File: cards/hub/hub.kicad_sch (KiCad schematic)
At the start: 28 parts, among them J1 USB_B, J2 BUS, J3 BUS

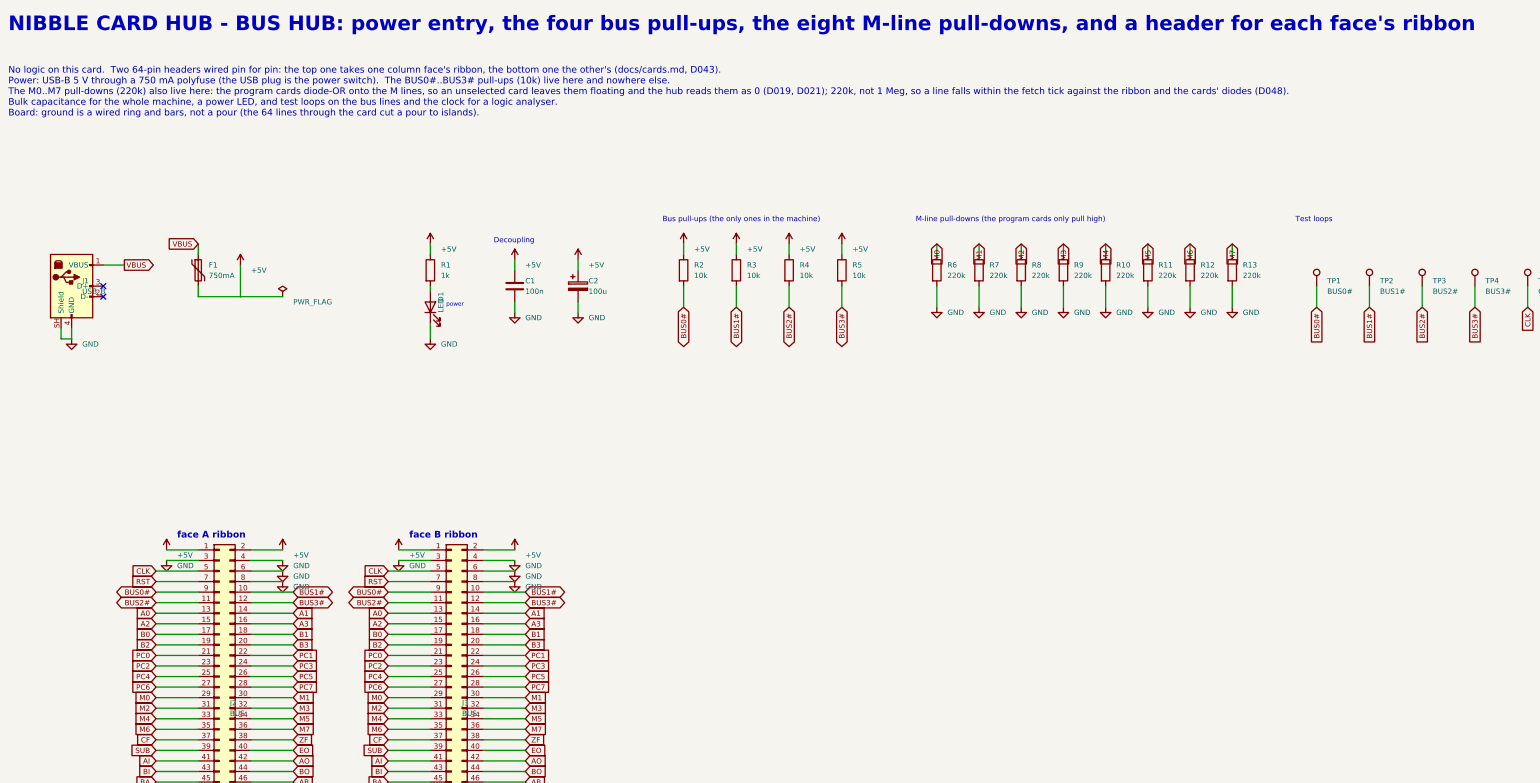
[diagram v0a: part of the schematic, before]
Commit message: Hub: bench-supply screw terminal and a 1.5 A polyfuse (D052)
The machine as built draws up to about 1.2 A (281 LEDs behind 1k, plus
the pull-ups), more than the 750 mA fuse and a computer's USB port were
ever going to carry. The hub now takes 5 V from a 5.08 mm screw terminal
on its left edge (the Kungber bench supply, 5.0 V with the limit at
1.5 A) as well as from the USB-B socket, both through a Bel 0ZRE0150FF
1.5 A polyfuse.

Routed with freerouting 2.4.1: 1.9 put an M5 via inside the 0.35 mm
bundle of the 64 bus lines and shorted M4/M5/M7 on two runs. KiCad DRC
and the JLCPCB-minimum DRC (0.127 track/space, 0.3/0.5 via, 0.5
hole-to-hole) both report no errors and nothing unconnected. Renders
checked. Parts table in order-1.md regenerated from bom.py (it had
also drifted from earlier card changes); bring-up, cards.md, README and
DECISIONS updated. The sim netlist is untouched (both parts are
sim=False), so the whole-machine proof stands.

Co-Authored-By: Claude Fable 5.1 <noreply@anthropic.com>
Claude-Session: https://claude.ai/code/session_01RktbhdQjDu7SpFpvkevyUU
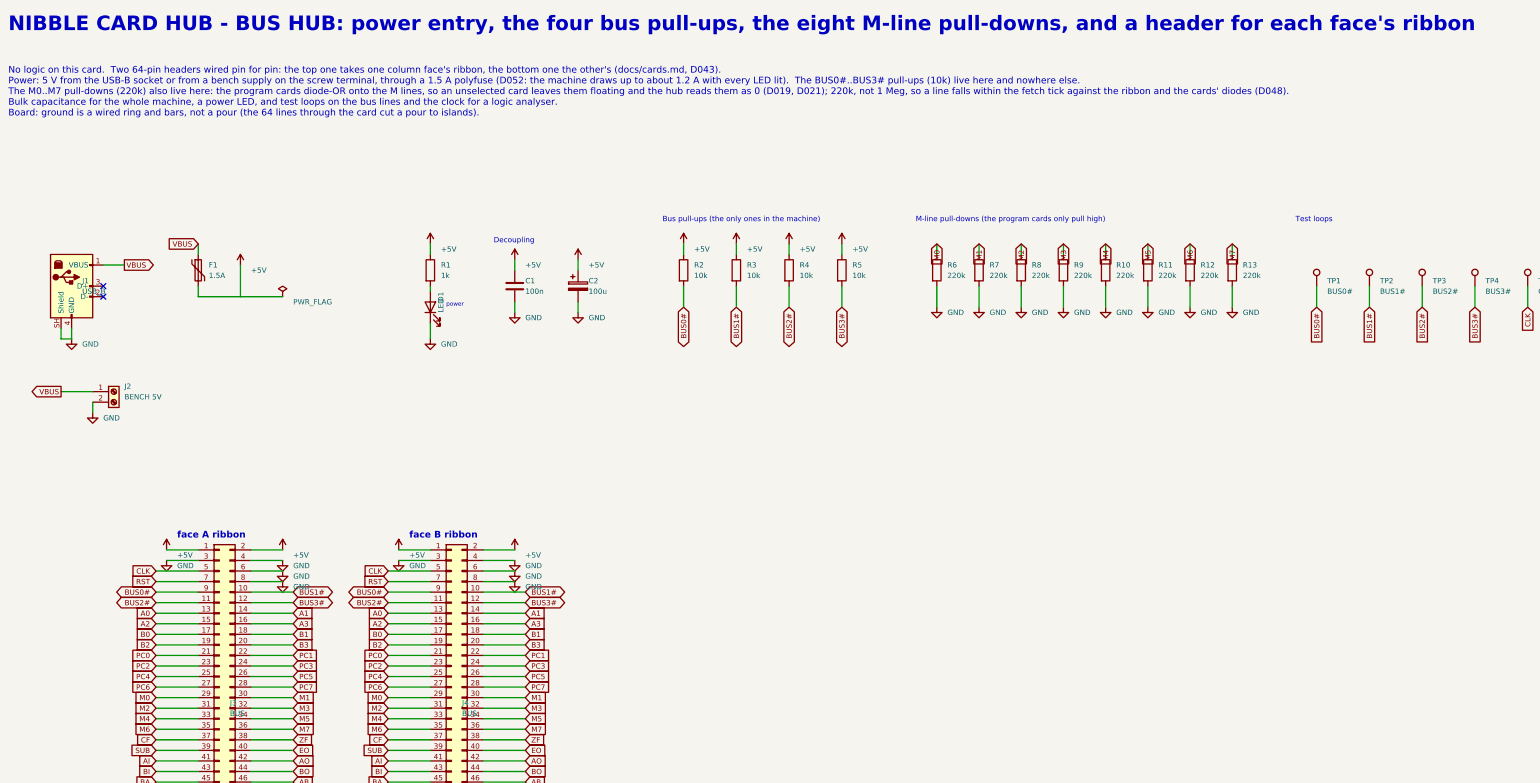
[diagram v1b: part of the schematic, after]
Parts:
- removed J2: BUS, Connector_IDC:IDC-Header_2x32_P2.54mm_Vertical, symbol Connector_Generic:Conn_02x32_Odd_Even
- added J2: BENCH 5V, TerminalBlock_Phoenix:TerminalBlock_Phoenix_MKDS-1,5-2-5.08_1x02_P5.08mm_Horizontal, symbol Connector:Screw_Terminal_01x02
- added J4: BUS, Connector_IDC:IDC-Header_2x32_P2.54mm_Vertical, symbol Connector_Generic:Conn_02x32_Odd_Even
- F1: value 750mA -> 1.5A; footprint Fuse:Fuse_BelFuse_0ZRE0075FF_L11.5mm_W4.8mm -> Fuse:Fuse_BelFuse_0ZRE0150FF_L23.4mm_W5.3mm
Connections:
- net +5V: now also J4.1 (Pin_1), J4.2 (Pin_2), J4.63 (Pin_63)
- net A0: now also J4.13 (Pin_13)
- net A1: now also J4.14 (Pin_14)
- net A2: now also J4.15 (Pin_15)
- net A3: now also J4.16 (Pin_16)
- net AB: now also J4.46 (Pin_46)
- net AI: now also J4.41 (Pin_41)
- net AO: now also J4.42 (Pin_42)
- net B0: now also J4.17 (Pin_17)
- net B1: now also J4.18 (Pin_18)
- net B2: now also J4.19 (Pin_19)
- net B3: now also J4.20 (Pin_20)
- net BA: now also J4.45 (Pin_45)
- net BI: now also J4.43 (Pin_43)
- net BO: now also J4.44 (Pin_44)
- net BUS0#: now also J4.9 (Pin_9)
- net BUS1#: now also J4.10 (Pin_10)
- net BUS2#: now also J4.11 (Pin_11)
- net BUS3#: now also J4.12 (Pin_12)
- net CF: now also J4.37 (Pin_37)
- net CLK: now also J4.5 (Pin_5)
- net EO: now also J4.40 (Pin_40)
- net F0: now also J4.60 (Pin_60)
- net F1: now also J4.61 (Pin_61)
- net FI: now also J4.52 (Pin_52)
- net GND: now also J2.2 (Pin_2), J4.3 (Pin_3), J4.4 (Pin_4), J4.6 (Pin_6), J4.64 (Pin_64), J4.8 (Pin_8)
- net HLT: now also J4.53 (Pin_53)
- net II: now also J4.49 (Pin_49)
- net INP: now also J4.62 (Pin_62)
- net IO: now also J4.48 (Pin_48)
- net M0: now also J4.29 (Pin_29)
- net M1: now also J4.30 (Pin_30)
- net M2: now also J4.31 (Pin_31)
- net M3: now also J4.32 (Pin_32)
- net M4: now also J4.33 (Pin_33)
- net M5: now also J4.34 (Pin_34)
- net M6: now also J4.35 (Pin_35)
- net M7: now also J4.36 (Pin_36)
- net MAI: now also J4.54 (Pin_54)
- net MI: now also J4.55 (Pin_55)
- net MO: now also J4.56 (Pin_56)
- net OI: now also J4.47 (Pin_47)
- net ONE: now also J4.59 (Pin_59)
- net PC0: now also J4.21 (Pin_21)
- net PC1: now also J4.22 (Pin_22)
- net PC2: now also J4.23 (Pin_23)
- net PC3: now also J4.24 (Pin_24)
- net PC4: now also J4.25 (Pin_25)
- net PC5: now also J4.26 (Pin_26)
- net PC6: now also J4.27 (Pin_27)
- net PC7: now also J4.28 (Pin_28)
- net PCE: now also J4.50 (Pin_50)
- net PCL: now also J4.51 (Pin_51)
- net RST: now also J4.7 (Pin_7)
- net SUB: now also J4.39 (Pin_39)
- net VBUS: now also J2.1 (Pin_1)
- net WRH: now also J4.58 (Pin_58)
- net WRL: now also J4.57 (Pin_57)
- net ZF: now also J4.38 (Pin_38)
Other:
- note added: "No logic on this card. Two 64-pin headers wired pin for pin: the top one takes one column face's ribbon, the bottom one the other's (docs/cards.md, D043). Power: 5 V from the USB-B socket or from a bench supply on the screw terminal, through a 1.5 A polyfuse (D052: the machine draws up to about 1.2 A with every LED lit). The BUS0#..BUS3# pull-ups (10k) live here and nowhere else. The M0..M7 pull-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"
- note removed: "No logic on this card. Two 64-pin headers wired pin for pin: the top one takes one column face's ribbon, the bottom one the other's (docs/cards.md, D043). Power: USB-B 5 V through a 750 mA polyfuse (the USB plug is the power switch). The BUS0#..BUS3# pull-ups (10k) live here and nowhere else. The M0..M7 pull-downs (220k) also live here: the program cards diode-OR onto the M lines, so an unselecte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"

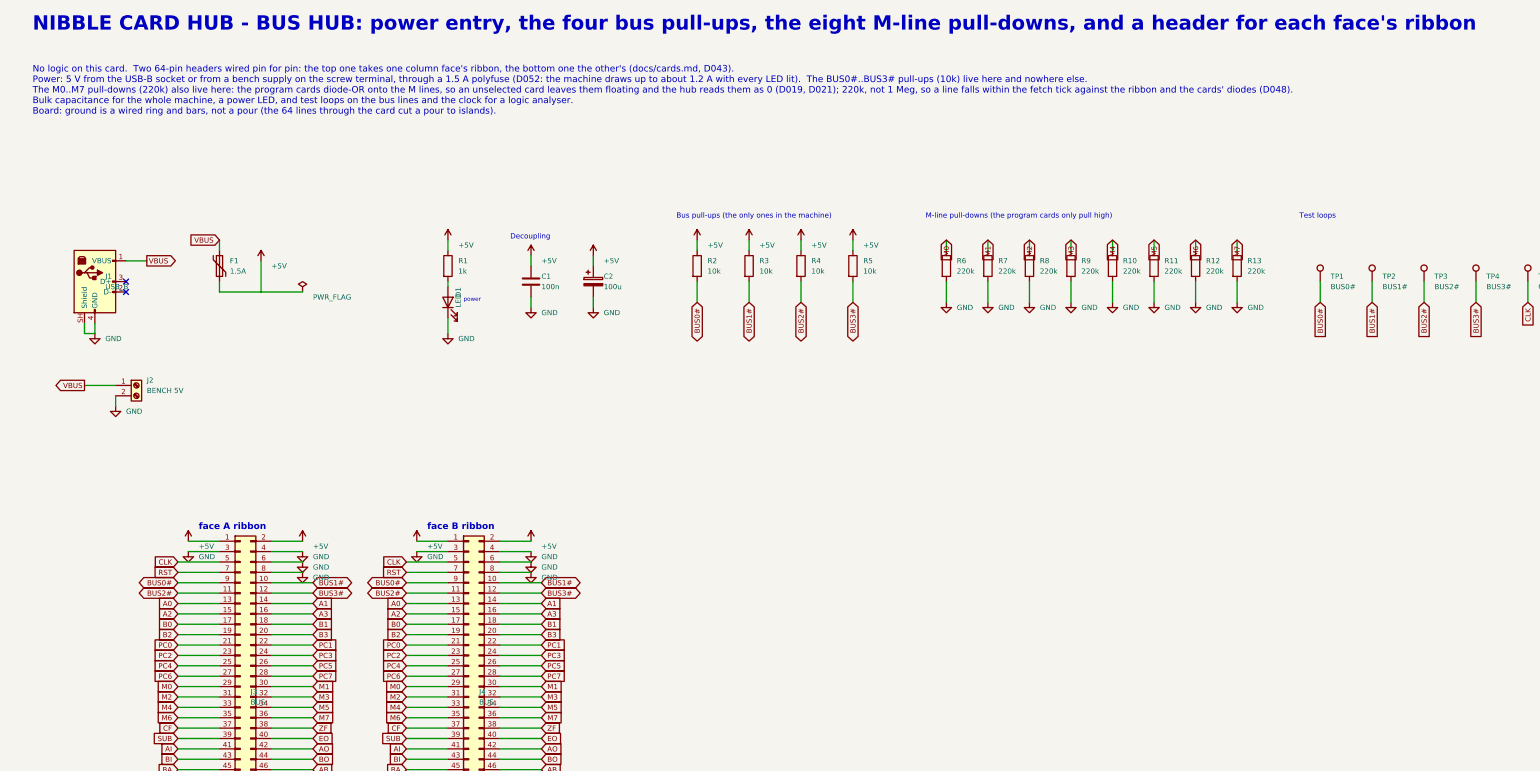
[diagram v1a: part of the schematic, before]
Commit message: Hub: the USB socket is gone (D057), the bench terminal is the only power entry
The machine is powered from the bench supply and nothing else, decided
with the pilot order on 2026-09-14; a socket nobody will plug in was a
part to buy, solder and explain, and a second path into the +5V rail.
The screw terminal moves up into the socket's place at the left edge,
its VBUS run to the 1.5 A polyfuse and its ground to the ring pre-routed
as before (the ground run past the top header's pin 1 at 0.5 mm: at
0.8 it broke the 0.15 mm clearance). The face-A silk label sits above
the terminal, clear of the fuse's body it used to run under. ERC 0,
freerouting 2.4.1 in one pass, DRC 0 errors, 0 open, clean under
JLCPCB's minimum rules.

Docs: DECISIONS D057 (supersedes the USB half of D052 and D015, the plug
as the switch); bring-up.md section 2 and the tools list without the
USB; cards/README.md, cards.md; order-1.md parts tables regenerated
(pilot 319, machine 7128).

Co-Authored-By: Claude Fable 5.1 <noreply@anthropic.com>
Claude-Session: https://claude.ai/code/session_01RktbhdQjDu7SpFpvkevyUU
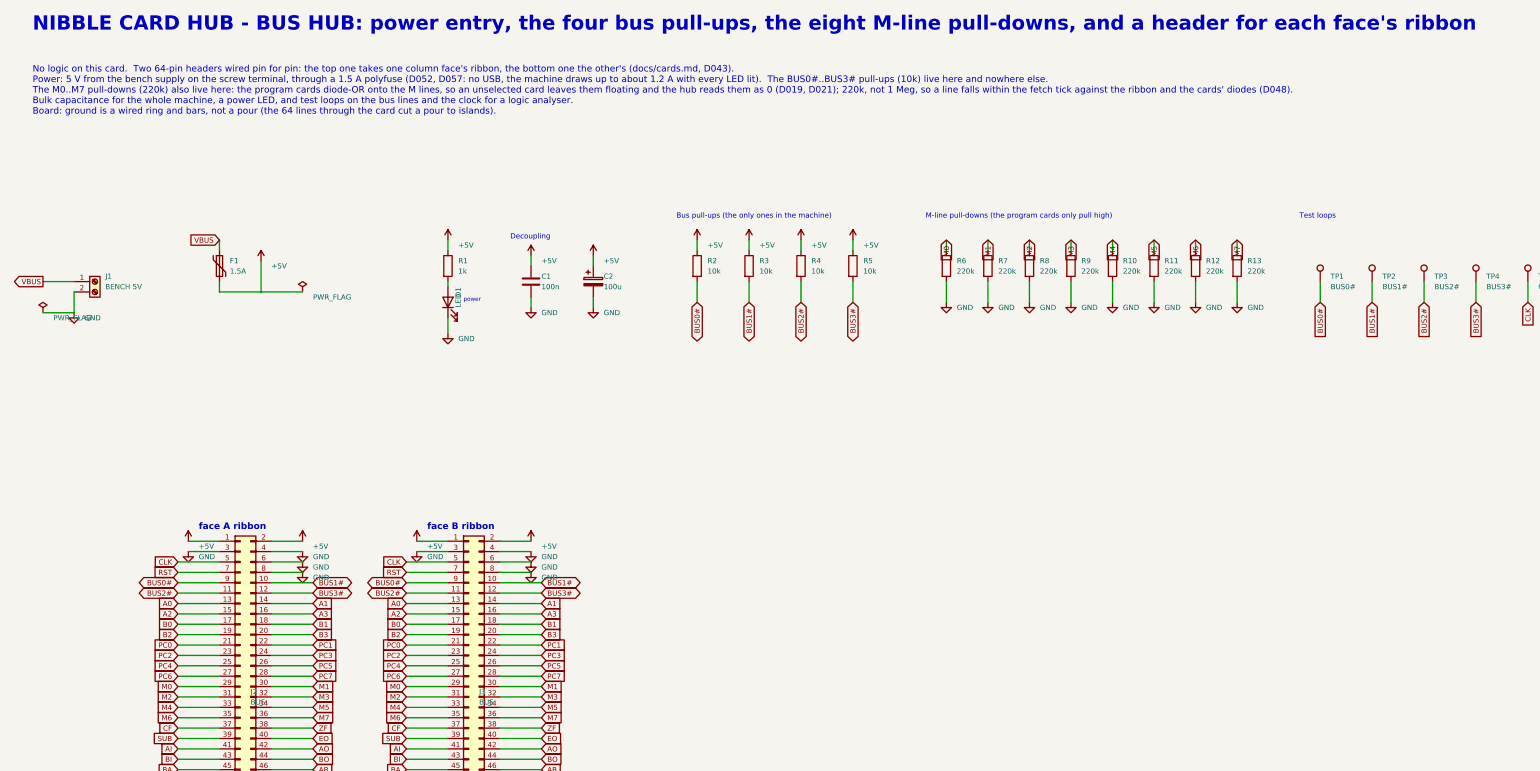
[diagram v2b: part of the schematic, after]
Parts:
- removed J1: USB_B, Connector_USB:USB_B_OST_USB-B1HSxx_Horizontal, symbol Connector:USB_B
- removed J2: BENCH 5V, TerminalBlock_Phoenix:TerminalBlock_Phoenix_MKDS-1,5-2-5.08_1x02_P5.08mm_Horizontal, symbol Connector:Screw_Terminal_01x02
- removed J4: BUS, Connector_IDC:IDC-Header_2x32_P2.54mm_Vertical, symbol Connector_Generic:Conn_02x32_Odd_Even
- added J1: BENCH 5V, TerminalBlock_Phoenix:TerminalBlock_Phoenix_MKDS-1,5-2-5.08_1x02_P5.08mm_Horizontal, symbol Connector:Screw_Terminal_01x02
- added J2: BUS, Connector_IDC:IDC-Header_2x32_P2.54mm_Vertical, symbol Connector_Generic:Conn_02x32_Odd_Even
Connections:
- net +5V: now also J2.1 (Pin_1), J2.2 (Pin_2), J2.63 (Pin_63)
- net A0: now also J2.13 (Pin_13)
- net A1: now also J2.14 (Pin_14)
- net A2: now also J2.15 (Pin_15)
- net A3: now also J2.16 (Pin_16)
- net AB: now also J2.46 (Pin_46)
- net AI: now also J2.41 (Pin_41)
- net AO: now also J2.42 (Pin_42)
- net B0: now also J2.17 (Pin_17)
- net B1: now also J2.18 (Pin_18)
- net B2: now also J2.19 (Pin_19)
- net B3: now also J2.20 (Pin_20)
- net BA: now also J2.45 (Pin_45)
- net BI: now also J2.43 (Pin_43)
- net BO: now also J2.44 (Pin_44)
- net BUS0#: now also J2.9 (Pin_9)
- net BUS1#: now also J2.10 (Pin_10)
- net BUS2#: now also J2.11 (Pin_11)
- net BUS3#: now also J2.12 (Pin_12)
- net CF: now also J2.37 (Pin_37)
- net CLK: now also J2.5 (Pin_5)
- net EO: now also J2.40 (Pin_40)
- net F0: now also J2.60 (Pin_60)
- net F1: now also J2.61 (Pin_61)
- net FI: now also J2.52 (Pin_52)
- net GND: now also J1.2 (Pin_2), J2.3 (Pin_3), J2.4 (Pin_4), J2.6 (Pin_6), J2.64 (Pin_64), J2.8 (Pin_8)
- net HLT: now also J2.53 (Pin_53)
- net II: now also J2.49 (Pin_49)
- net INP: now also J2.62 (Pin_62)
- net IO: now also J2.48 (Pin_48)
- net M0: now also J2.29 (Pin_29)
- net M1: now also J2.30 (Pin_30)
- net M2: now also J2.31 (Pin_31)
- net M3: now also J2.32 (Pin_32)
- net M4: now also J2.33 (Pin_33)
- net M5: now also J2.34 (Pin_34)
- net M6: now also J2.35 (Pin_35)
- net M7: now also J2.36 (Pin_36)
- net MAI: now also J2.54 (Pin_54)
- net MI: now also J2.55 (Pin_55)
- net MO: now also J2.56 (Pin_56)
- net OI: now also J2.47 (Pin_47)
- net ONE: now also J2.59 (Pin_59)
- net PC0: now also J2.21 (Pin_21)
- net PC1: now also J2.22 (Pin_22)
- net PC2: now also J2.23 (Pin_23)
- net PC3: now also J2.24 (Pin_24)
- net PC4: now also J2.25 (Pin_25)
- net PC5: now also J2.26 (Pin_26)
- net PC6: now also J2.27 (Pin_27)
- net PC7: now also J2.28 (Pin_28)
- net PCE: now also J2.50 (Pin_50)
- net PCL: now also J2.51 (Pin_51)
- net RST: now also J2.7 (Pin_7)
- net SUB: now also J2.39 (Pin_39)
- net VBUS: now also J1.1 (Pin_1)
- net WRH: now also J2.58 (Pin_58)
- net WRL: now also J2.57 (Pin_57)
- net ZF: now also J2.38 (Pin_38)
- no-connect marks 2 -> 0
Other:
- note added: "No logic on this card. Two 64-pin headers wired pin for pin: the top one takes one column face's ribbon, the bottom one the other's (docs/cards.md, D043). Power: 5 V from the bench supply on the screw terminal, through a 1.5 A polyfuse (D052, D057: no USB, the machine draws up to about 1.2 A with every LED lit). The BUS0#..BUS3# pull-ups (10k) live here and nowhere else. The M0..M7 pull-downs (22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"
- note removed: "No logic on this card. Two 64-pin headers wired pin for pin: the top one takes one column face's ribbon, the bottom one the other's (docs/cards.md, D043). Power: 5 V from the USB-B socket or from a bench supply on the screw terminal, through a 1.5 A polyfuse (D052: the machine draws up to about 1.2 A with every LED lit). The BUS0#..BUS3# pull-ups (10k) live here and nowhere else. The M0..M7 pull-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"
